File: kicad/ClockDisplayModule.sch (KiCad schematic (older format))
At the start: 11 parts

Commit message: Library correction and rework of schematic
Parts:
- removed C? (x2): C, symbol C
- removed D? (x4): LED, symbol LED
- removed R?: R, symbol R
- added C?: 0.1u, symbol C
- added C?: 10u, symbol CP
- added D? (x4): LED, symbol LED
- added P?: CONN_01X05, symbol CONN_01X05
- added R?: 25K, symbol R
- added U?: MAX7221, symbol MAX7221
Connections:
- net labels added: CLK, Dig_0, Dig_1, Dig_2, Dig_3, MOSI, Seg_A, Seg_B, Seg_C, Seg_D, Seg_E, Seg_F, Seg_G, Signal, ~SS
- net labels removed: Dig0, Dig1, Dig2, Dig3, segA, segB, segC, segD, segDP, segE, segF, segG
- wire segments 75 -> 91
- no-connect marks 3 -> 9
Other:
- moved on the sheet: AFF?

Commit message: Initial layout
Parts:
- removed C?: 10u, symbol CP
- added C101: 10u, Capacitors_SMD:c_elec_4x5.8, symbol CP
- AFF101, AFF102, AFF103, AFF104: renamed from AFF?; footprint (none) -> ClockFootprints:SC08-11SURKWA; ConradPN (none) -> 1050566 - 62; Label (none) -> Value; Link (none) -> http://www.conrad.de/ce/de/product/1050566/7-Segment-Anzeig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; MPN (none) -> SC08-11SURKWA
- C102: renamed from C?; footprint (none) -> Capacitors_SMD:C_0805_HandSoldering
- D101: renamed from D?; value LED -> Colon1; footprint (none) -> LEDs:LED-0805
- D102: renamed from D?; value LED -> Colon2; footprint (none) -> LEDs:LED-0805
- D103: renamed from D?; value LED -> Alarm; footprint (none) -> LEDs:LED-0805
- D104: renamed from D?; value LED -> Auto; footprint (none) -> LEDs:LED-0805
- P101: renamed from P?; footprint (none) -> Pin_Headers:Pin_Header_Straight_1x05
- R101: renamed from R?; footprint (none) -> Resistors_SMD:R_0805_HandSoldering
- U101: renamed from U?; footprint (none) -> SMD_Packages:SOIC-24; ConradPN (none) -> 170137 - 62; Label (none) -> Value; Link (none) -> http://www.conrad.de/ce/de/product/170137/Linear-IC-Maxim-I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; MPN (none) -> MAX7221
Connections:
- net GND: now also C101.2
- net V+: now also C101.1
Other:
- moved on the sheet: C102, R101

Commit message: Small changes to schematic
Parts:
- D101: Label Colon1 -> (none)
- D102: Label Colon 2 -> (none)
- D103: Label Alarm_Enabled -> (none)
- D104: Label Auto_Time -> (none)
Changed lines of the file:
@@
 	5700 2300 5800 2400
 Entry Wire Line
-	5700 1500 5800 1600
-Entry Wire Line
-	5700 1400 5800 1500
-Entry Wire Line
-	5700 1300 5800 1400
-Entry Wire Line
-	5700 1200 5800 1300
-Entry Wire Line
-	5700 1100 5800 1200
-Entry Wire Line
-	5700 1000 5800 1100
-Entry Wire Line
-	5700 900  5800 1000
+	5700 1700 5800 1600
+Entry Wire Line
+	5700 1600 5800 1500
+Entry Wire Line
+	5700 1500 5800 1400
+Entry Wire Line
+	5700 1400 5800 1300
+Entry Wire Line
+	5700 1300 5800 1200
+Entry Wire Line
+	5700 1200 5800 1100
+Entry Wire Line
+	5700 1100 5800 1000
 NoConn ~ 3600 4150
 NoConn ~ 3600 4250
@@
 P 4450 4900
 F 0 "D101" H 4450 5000 50  0000 C CNN
-F 1 "Colon1" H 4450 4800 50  0001 C CNN
+F 1 "Colon1" H 4450 4800 50  0000 C CNN
 F 2 "LEDs:LED-0805" H 4450 4900 60  0001 C CNN
 F 3 "" H 4450 4900 60  0000 C CNN
 F 4 "Value" H 4450 4900 60  0001 C CNN "MPN"
 F 5 "Value" H 4450 4900 60  0001 C CNN "ConradPN"
-F 6 "Colon1" H 4450 4750 60  0000 C CNN "Label"
 	1    4450 4900
 	-1   0    0    1
@@
 P 4450 5200
 F 0 "D102" H 4450 5300 50  0000 C CNN
-F 1 "Colon2" H 4450 5100 50  0001 C CNN
+F 1 "Colon2" H 4450 5100 50  0000 C CNN
 F 2 "LEDs:LED-0805" H 4450 5200 60  0001 C CNN
 F 3 "" H 4450 5200 60  0000 C CNN
 F 4 "Value" H 4450 5200 60  0001 C CNN "MPN"
 F 5 "Value" H 4450 5200 60  0001 C CNN "ConradPN"
-F 6 "Colon 2" H 4450 5100 60  0000 C CNN "Label"
 	1    4450 5200
 	-1   0    0    1
@@
 P 4450 5750
 F 0 "D103" H 4450 5850 50  0000 C CNN
-F 1 "Alarm" H 4450 5650 50  0001 C CNN
+F 1 "Alarm" H 4450 5650 50  0000 C CNN
 F 2 "LEDs:LED-0805" H 4450 5750 60  0001 C CNN
 F 3 "" H 4450 5750 60  0000 C CNN
 F 4 "Value" H 4450 5750 60  0001 C CNN "MPN"
 F 5 "Value" H 4450 5750 60  0001 C CNN "ConradPN"
-F 6 "Alarm_Enabled" H 4450 5600 60  0000 C CNN "Label"
 	1    4450 5750
 	-1   0    0    1
@@
 P 4450 6100
 F 0 "D104" H 4450 6200 50  0000 C CNN
-F 1 "Auto" H 4450 6000 50  0001 C CNN
+F 1 "Auto" H 4450 6000 50  0000 C CNN
 F 2 "LEDs:LED-0805" H 4450 6100 60  0001 C CNN
 F 3 "" H 4450 6100 60  0000 C CNN
 F 4 "Value" H 4450 6100 60  0001 C CNN "MPN"
 F 5 "Value" H 4450 6100 60  0001 C CNN "ConradPN"
-F 6 "Auto_Time" H 4450 5950 60  0000 C CNN "Label"
 	1    4450 6100
 	-1   0    0    1
@@
 Text GLabel 2150 1350 0    60   Input ~ 0
 GND
-Wire Wire Line
-	2300 1950 2300 2250
-Wire Wire Line
-	2300 2950 1250 2950
-Wire Wire Line
-	1250 2950 1250 2700
-Wire Wire Line
-	1950 2600 1950 2400
-Wire Wire Line
-	2800 4900 2800 5100
-Connection ~ 2800 5000
-Wire Wire Line
-	1950 3400 2300 3400
-Wire Wire Line
-	1950 3550 2300 3550
-Wire Wire Line
-	1950 3700 2300 3700
-Wire Wire Line
-	3600 2650 3950 2650
-Wire Wire Line
-	3600 2750 3950 2750
-Wire Wire Line
-	3600 2850 3950 2850
-Wire Wire Line
-	3600 2950 3950 2950
-Wire Wire Line
-	3600 3050 3950 3050
-Wire Wire Line
-	3600 3150 3950 3150
-Wire Wire Line
-	3600 3250 3950 3250
-Wire Wire Line
-	6100 1000 5800 1000
-Wire Wire Line
-	6100 1100 5800 1100
-Wire Wire Line
-	6100 1200 5800 1200
-Wire Wire Line
-	6100 1300 5800 1300
-Wire Wire Line
-	6100 1400 5800 1400
-Wire Wire Line
-	6100 1500 5800 1500
-Wire Wire Line
-	6100 1600 5800 1600
-Wire Wire Line
-	6100 2400 5800 2400
-Wire Wire Line
-	6100 2500 5800 2500
-Wire Wire Line
-	6100 2600 5800 2600
-Wire Wire Line
-	6100 2700 5800 2700
-Wire Wire Line
-	6100 2800 5800 2800
-Wire Wire Line
-	6100 2900 5800 2900
-Wire Wire Line
-	6100 3000 5800 3000
-Wire Wire Line
-	6100 3900 5800 3900
-Wire Wire Line
-	6100 4000 5800 4000
-Wire Wire Line
-	6100 4100 5800 4100
-Wire Wire Line
-	6100 4200 5800 4200
-Wire Wire Line
-	6100 4300 5800 4300
-Wire Wire Line
-	6100 4400 5800 4400
-Wire Wire Line
-	6100 4500 5800 4500
-Wire Wire Line
-	6100 5200 5800 5200
-Wire Wire Line
-	6100 5300 5800 5300
-Wire Wire Line
-	6100 5400 5800 5400
-Wire Wire Line
-	6100 5500 5800 5500
-Wire Wire Line
-	6100 5600 5800 5600
-Wire Wire Line
-	6100 5700 5800 5700
-Wire Wire Line
-	6100 5800 5800 5800
-Wire Wire Line
-	7300 2450 7700 2450
-Wire Wire Line
-	7300 3950 7700 3950
-Wire Wire Line
-	7300 5250 7700 5250
-Wire Wire Line
-	7300 950  8000 950
-Wire Wire Line
-	7750 1050 7750 950
-Connection ~ 7750 950
-Wire Wire Line
-	7700 2450 7700 2350
-Connection ~ 7700 2350
-Wire Wire Line
-	7700 3950 7700 3850
-Connection ~ 7700 3850
-Wire Wire Line
-	7700 5250 7700 5150
-Connection ~ 7700 5150
-Wire Wire Line
-	3600 3950 3850 3950
-Wire Bus Line
-	5700 900  5700 5700
-Wire Wire Line
-	5100 1550 5600 1550
-Wire Wire Line
-	5100 1650 5600 1650
-Wire Wire Line
-	5100 1750 5600 1750
-Wire Wire Line
-	5100 1850 5600 1850
-Wire Wire Line
-	5100 1950 5600 1950
-Wire Wire Line
-	5100 2050 5600 2050
-Wire Wire Line
-	5100 2150 5600 2150
-Wire Wire Line
-	4650 4900 4950 4900
-Wire Wire Line
-	4950 4900 4950 6450
-Wire Wire Line
-	4950 6450 5250 6450
-Wire Wire Line
-	4650 5200 4950 5200
-Connection ~ 4950 5200
-Wire Wire Line
-	4650 5750 4950 5750
-Connection ~ 4950 5750
-Wire Wire Line
-	4650 6100 4950 6100
-Connection ~ 4950 6100
-Wire Wire Line
-	3900 4900 4250 4900
-Wire Wire Line
-	3900 5200 4250 5200
-Wire Wire Line
-	3900 5750 4250 5750
-Wire Wire Line
-	3900 6100 4250 6100
-Wire Wire Line
-	2150 950  2500 950
-Wire Wire Line
-	2150 1050 2500 1050
-Wire Wire Line
-	2150 1150 2500 1150
-Wire Wire Line
-	2150 1250 2500 1250
-Wire Wire Line
-	2150 1350 2500 1350
-Wire Wire Line
-	1050 1950 2300 1950
-Connection ~ 1650 1950
-Wire Wire Line
-	1950 2100 1950 1950
-Connection ~ 1950 1950
-Wire Wire Line
-	1250 2400 1250 1950
-Connection ~ 1250 1950
 $Comp
 L CP C101
@@
 $EndComp
 Wire Wire Line
+	2300 1950 2300 2250
+Wire Wire Line
+	2300 2950 1250 2950
+Wire Wire Line
+	1250 2950 1250 2700
+Wire Wire Line
+	1950 2600 1950 2400
+Wire Wire Line
+	2800 4900 2800 5100
+Connection ~ 2800 5000
+Wire Wire Line
+	1950 3400 2300 3400
+Wire Wire Line
+	1950 3550 2300 3550
+Wire Wire Line
+	1950 3700 2300 3700
+Wire Wire Line
+	3600 2650 3950 2650
+Wire Wire Line
+	3600 2750 3950 2750
+Wire Wire Line
+	3600 2850 3950 2850
+Wire Wire Line
+	3600 2950 3950 2950
+Wire Wire Line
+	3600 3050 3950 3050
+Wire Wire Line
+	3600 3150 3950 3150
+Wire Wire Line
+	3600 3250 3950 3250
+Wire Wire Line
+	6100 1000 5800 1000
+Wire Wire Line
+	6100 1100 5800 1100
+Wire Wire Line
+	6100 1200 5800 1200
+Wire Wire Line
+	6100 1300 5800 1300
+Wire Wire Line
+	6100 1400 5800 1400
+Wire Wire Line
+	6100 1500 5800 1500
+Wire Wire Line
+	6100 1600 5800 1600
+Wire Wire Line
+	6100 2400 5800 2400
+Wire Wire Line
+	6100 2500 5800 2500
+Wire Wire Line
+	6100 2600 5800 2600
+Wire Wire Line
+	6100 2700 5800 2700
+Wire Wire Line
+	6100 2800 5800 2800
+Wire Wire Line
+	6100 2900 5800 2900
+Wire Wire Line
+	6100 3000 5800 3000
+Wire Wire Line
+	6100 3900 5800 3900
+Wire Wire Line
+	6100 4000 5800 4000
+Wire Wire Line
+	6100 4100 5800 4100
+Wire Wire Line
+	6100 4200 5800 4200
+Wire Wire Line
+	6100 4300 5800 4300
+Wire Wire Line
+	6100 4400 5800 4400
+Wire Wire Line
+	6100 4500 5800 4500
+Wire Wire Line
+	6100 5200 5800 5200
+Wire Wire Line
+	6100 5300 5800 5300
+Wire Wire Line
+	6100 5400 5800 5400
+Wire Wire Line
+	6100 5500 5800 5500
+Wire Wire Line
+	6100 5600 5800 5600
+Wire Wire Line
+	6100 5700 5800 5700
+Wire Wire Line
+	6100 5800 5800 5800
+Wire Wire Line
+	7300 2450 7700 2450
+Wire Wire Line
+	7300 3950 7700 3950
+Wire Wire Line
+	7300 5250 7700 5250
+Wire Wire Line
+	7300 950  8000 950
+Wire Wire Line
+	7750 1050 7750 950
+Connection ~ 7750 950
+Wire Wire Line
+	7700 2450 7700 2350
+Connection ~ 7700 2350
+Wire Wire Line
+	7700 3950 7700 3850
+Connection ~ 7700 3850
+Wire Wire Line
+	7700 5250 7700 5150
+Connection ~ 7700 5150
+Wire Wire Line
+	3600 3950 3850 3950
+Wire Wire Line
+	5100 1550 5600 1550
+Wire Wire Line
+	5100 1650 5600 1650
+Wire Wire Line
+	5100 1750 5600 1750
+Wire Wire Line
+	5100 1850 5600 1850
+Wire Wire Line
+	5100 1950 5600 1950
+Wire Wire Line
+	5100 2050 5600 2050
+Wire Wire Line
+	5100 2150 5600 2150
+Wire Wire Line
+	4650 4900 4950 4900
+Wire Wire Line
+	4950 4900 4950 6450
+Wire Wire Line
+	4950 6450 5250 6450
+Wire Wire Line
+	4650 5200 4950 5200
+Connection ~ 4950 5200
+Wire Wire Line
+	4650 5750 4950 5750
+Connection ~ 4950 5750
+Wire Wire Line
+	4650 6100 4950 6100
+Connection ~ 4950 6100
+Wire Wire Line
+	3900 4900 4250 4900
+Wire Wire Line
+	3900 5200 4250 5200
+Wire Wire Line
+	3900 5750 4250 5750
+Wire Wire Line
+	3900 6100 4250 6100
+Wire Wire Line
+	2150 950  2500 950
+Wire Wire Line
+	2150 1050 2500 1050
+Wire Wire Line
+	2150 1150 2500 1150
+Wire Wire Line
+	2150 1250 2500 1250
+Wire Wire Line
+	2150 1350 2500 1350
+Wire Wire Line
+	1050 1950 2300 1950
+Connection ~ 1650 1950
+Wire Wire Line
+	1950 2100 1950 1950
+Connection ~ 1950 1950
+Wire Wire Line
+	1250 2400 1250 1950
+Connection ~ 1250 1950
+Wire Wire Line
 	1650 1950 1650 2100
 Wire Wire Line
@@
 Wire Wire Line
 	3100 5000 2800 5000
+Wire Bus Line
+	5700 1100 5700 5700
 $EndSCHEMATC

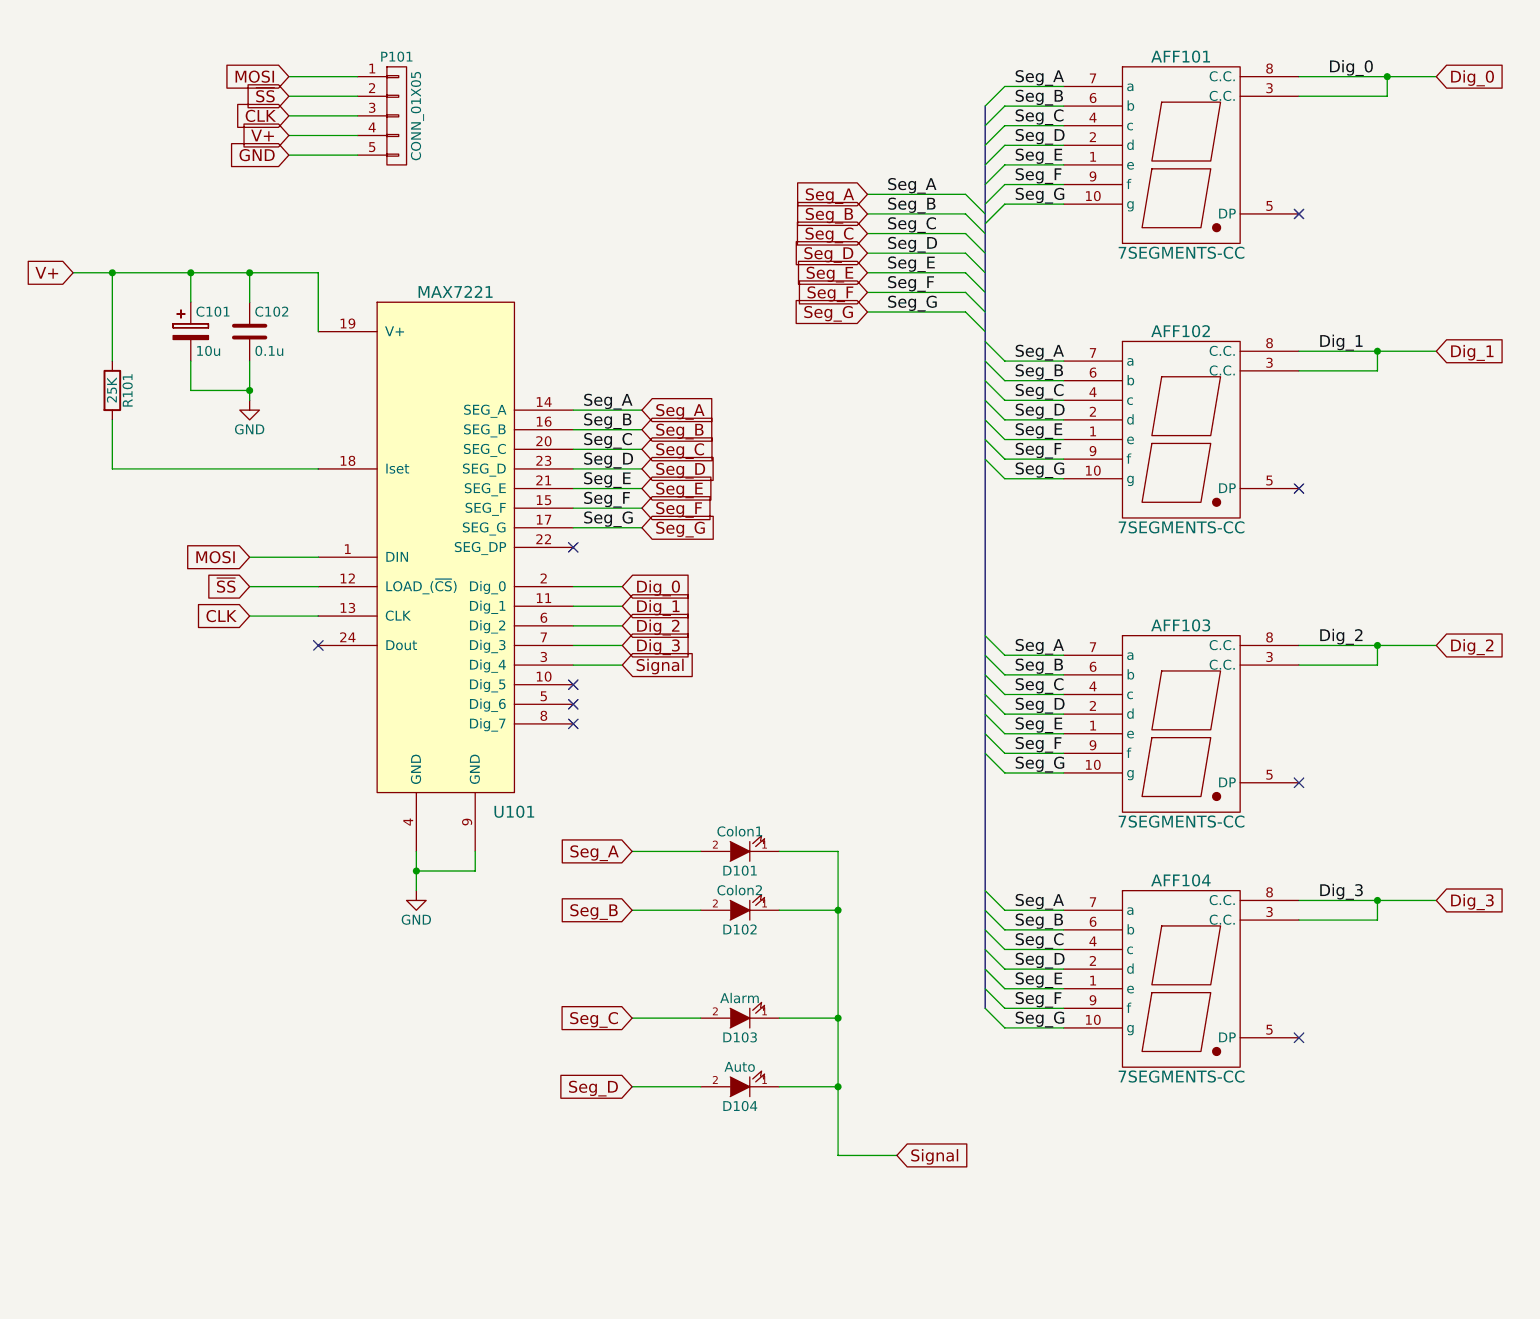
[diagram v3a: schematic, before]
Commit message: Initial trail of the layout. The given board is not big enough
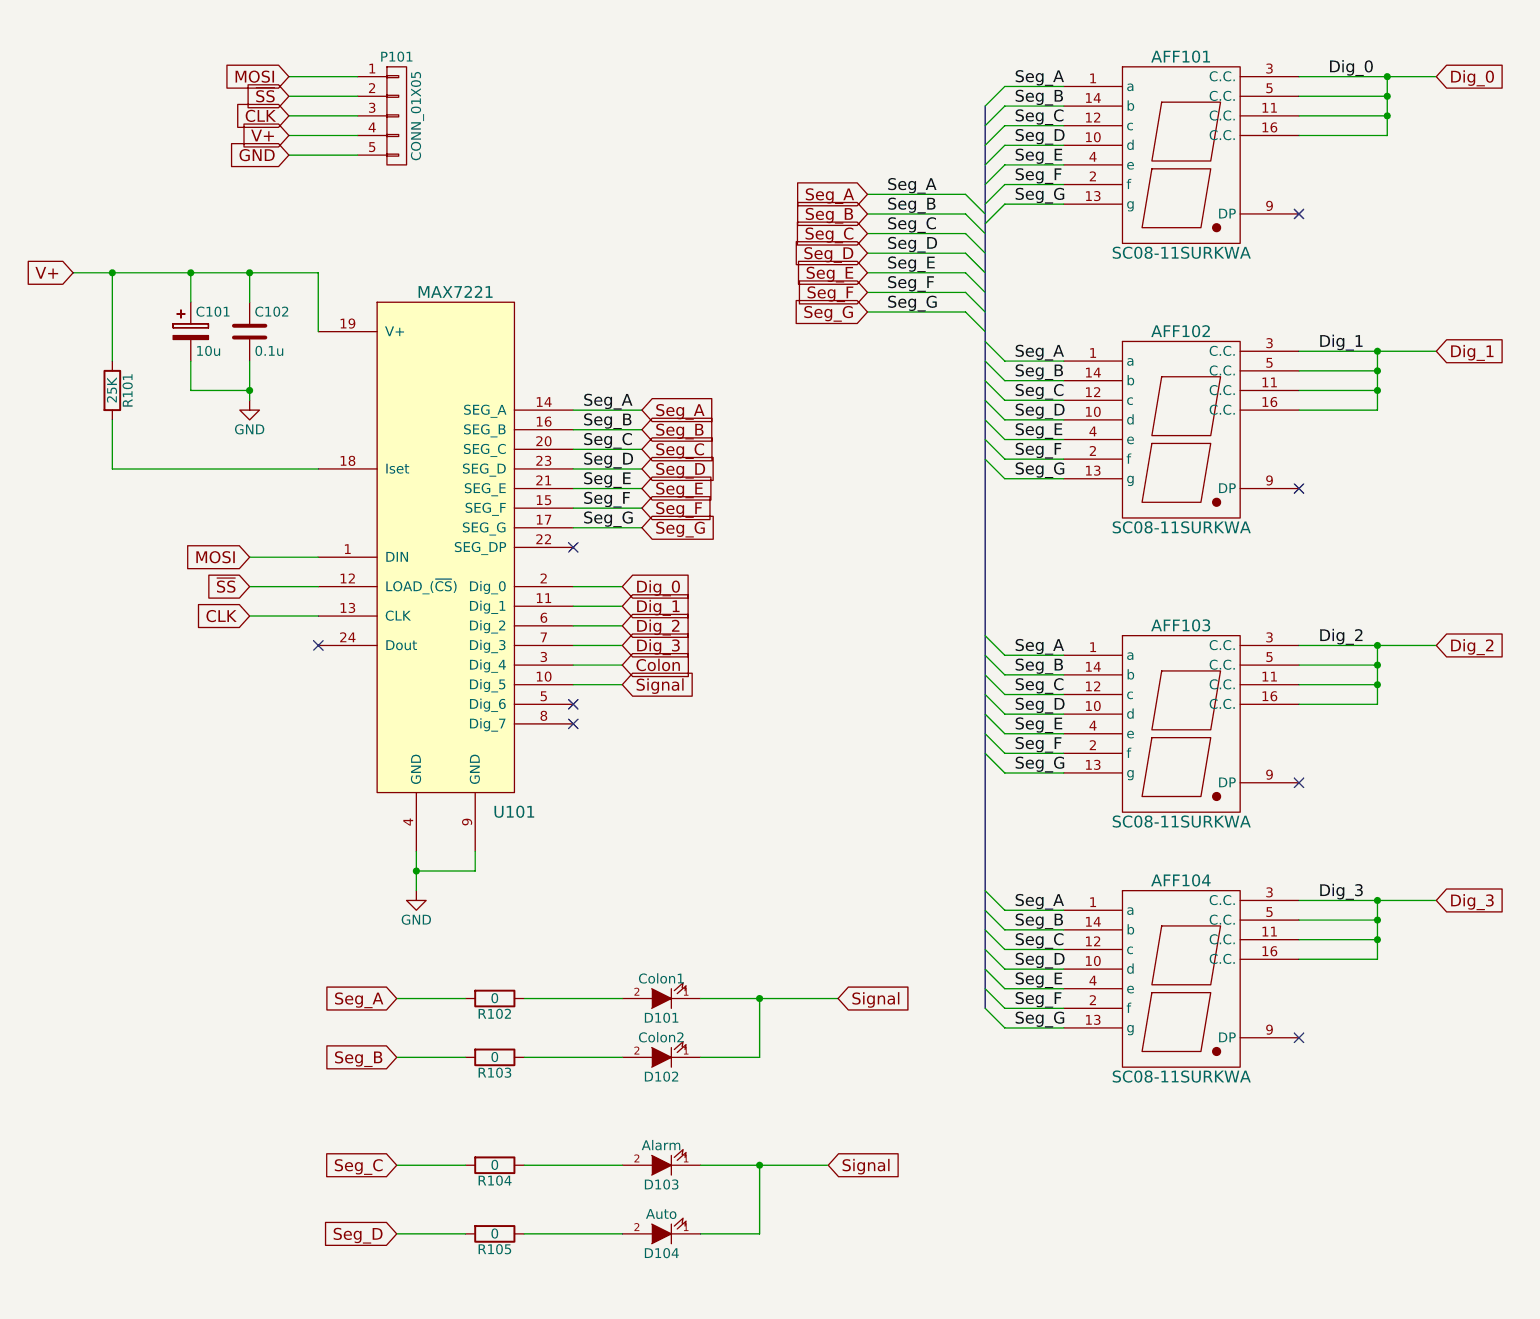
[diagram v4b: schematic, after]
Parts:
- removed AFF101, AFF102, AFF103, AFF104: 7SEGMENTS-CC, ClockFootprints:SC08-11SURKWA, symbol 7SEGMENTS-CC
- added AFF101, AFF102, AFF103, AFF104: SC08-11SURKWA, ClockFootprints:SC08-11SURKWA, symbol SC08-11SURKWA
- added R102, R103, R104, R105: 0, Resistors_SMD:R_0805_HandSoldering, symbol R
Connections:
- net Dig_0: now also AFF101.11 (C.C.), AFF101.16 (C.C.), AFF101.3 (C.C.), AFF101.5 (C.C.)
- net Dig_1: now also AFF102.11 (C.C.), AFF102.16 (C.C.), AFF102.3 (C.C.), AFF102.5 (C.C.)
- net Dig_2: now also AFF103.11 (C.C.), AFF103.16 (C.C.), AFF103.3 (C.C.), AFF103.5 (C.C.)
- net Dig_3: now also AFF104.11 (C.C.), AFF104.16 (C.C.), AFF104.3 (C.C.), AFF104.5 (C.C.)
- net Seg_A: now also AFF101.1 (a), AFF102.1 (a), AFF103.1 (a), AFF104.1 (a), R102.2; no longer D101.2 (A)
- net Seg_B: now also AFF101.14 (b), AFF102.14 (b), AFF103.14 (b), AFF104.14 (b), R103.2; no longer D102.2 (A)
- net Seg_C: now also AFF101.12 (c), AFF102.12 (c), AFF103.12 (c), AFF104.12 (c), R104.2; no longer D103.2 (A)
- net Seg_D: now also AFF101.10 (d), AFF102.10 (d), AFF103.10 (d), AFF104.10 (d), R105.2; no longer D104.2 (A)
- net Seg_E: now also AFF101.4 (e), AFF102.4 (e), AFF103.4 (e), AFF104.4 (e)
- net Seg_F: now also AFF101.2 (f), AFF102.2 (f), AFF103.2 (f), AFF104.2 (f)
- net Seg_G: now also AFF101.13 (g), AFF102.13 (g), AFF103.13 (g), AFF104.13 (g)
- net Signal: now also U101.10 (Dig_5); no longer U101.3 (Dig_4)
- new net: D101.2 (A), R102.1
- new net: D102.2 (A), R103.1
- new net: D103.2 (A), R104.1
- new net: D104.2 (A), R105.1
- new net Colon: U101.3 (Dig_4)
- no-connect marks 9 -> 8
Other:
- moved on the sheet: D101, D102, D103, D104
